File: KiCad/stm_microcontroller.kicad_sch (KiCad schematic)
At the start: 21 parts, among them J5 USB_C_Receptacle_USB2.0_14P, SW1 SW_Push, SW2 SW_Push, U1 STM32F103C8Tx, Y1 8Mhz

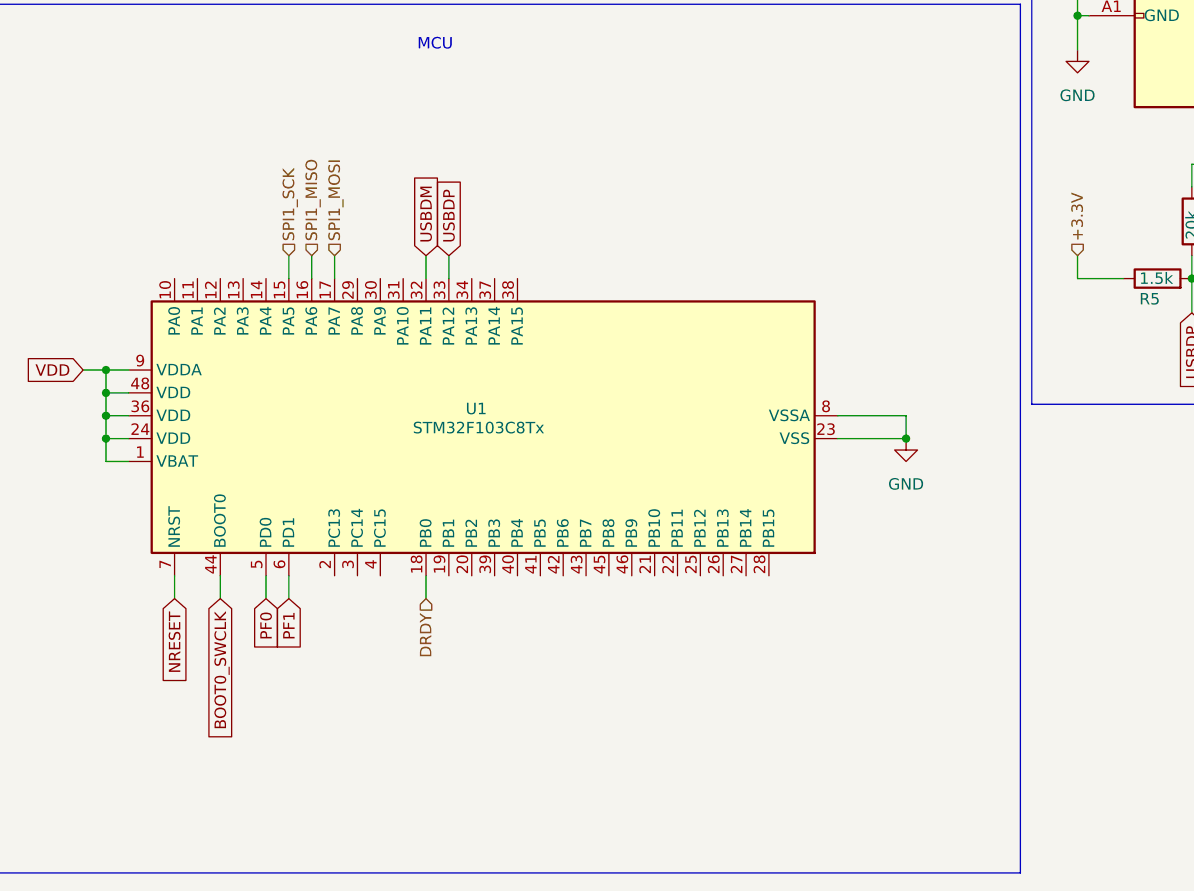
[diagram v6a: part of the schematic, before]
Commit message: Add Single Wire Debug
* Add Single Wire Debug (SWD) Tag Connect Connector
* Re-layout of 5V power so the 5V pins connect to a pad directly behind the USB connector
* Add 0R resistors to air gap the 3.3V and 5V power rails for incremental board bringup
* Rotate ADS1220 for cleaner layout
* Remove connections to reference voltage pins, since AVDD/AVSS is a valid reference

fixup

fixup

fixup
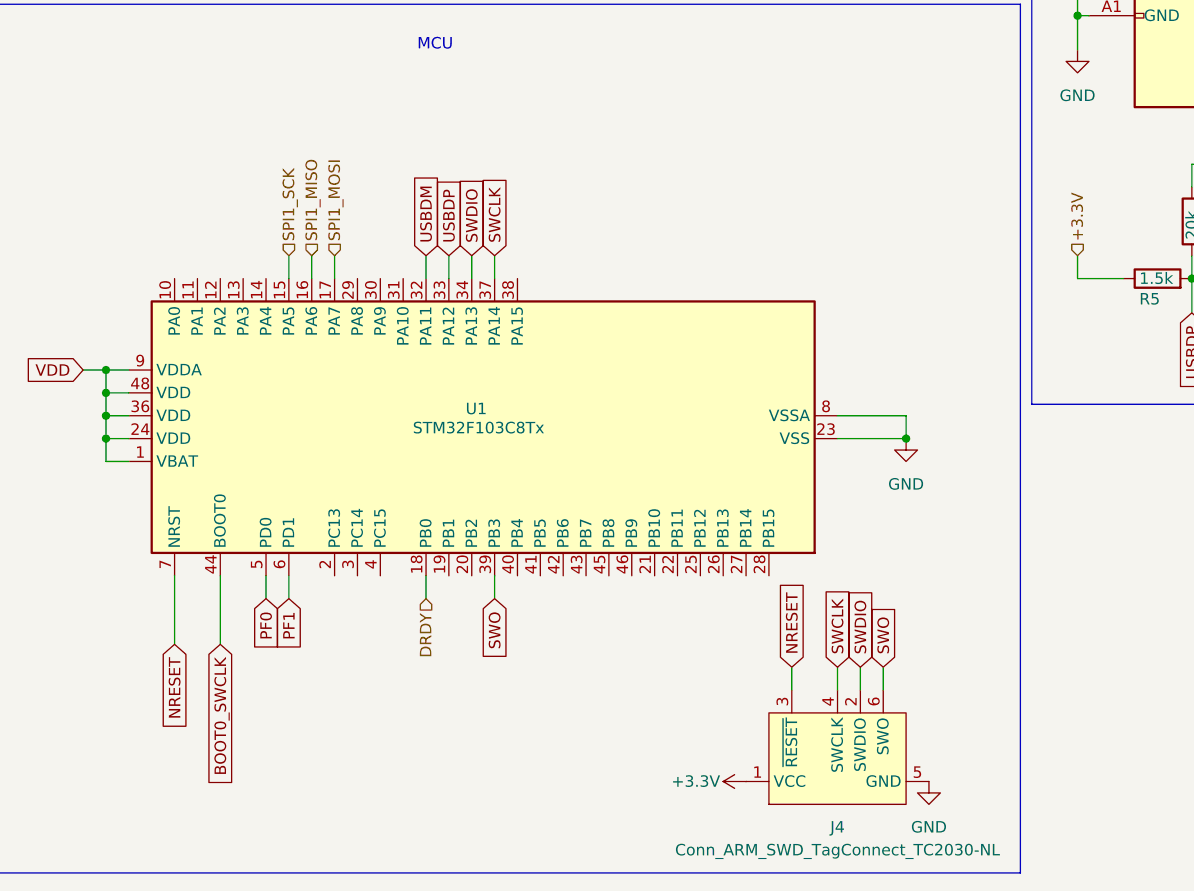
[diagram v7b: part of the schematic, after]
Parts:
- added J4: Conn_ARM_SWD_TagConnect_TC2030-NL, Connector:Tag-Connect_TC2030-IDC-NL_2x03_P1.27mm_Vertical, symbol Connector:Conn_ARM_SWD_TagConnect_TC2030-NL
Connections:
- net +3.3V: now also J4.1 (VCC)
- net GND: now also J4.5 (GND)
- net NRESET: now also J4.3 (~{RESET})
- net SWDIO: now reaches U1.34 (PA13)
- net SWDIO: now also J4.2 (SWDIO)
- net SWCLK: now reaches U1.37 (PA14)
- net SWCLK: now also J4.4 (SWCLK)
- net SWO: now reaches U1.39 (PB3)
- net SWO: now also J4.6 (SWO)

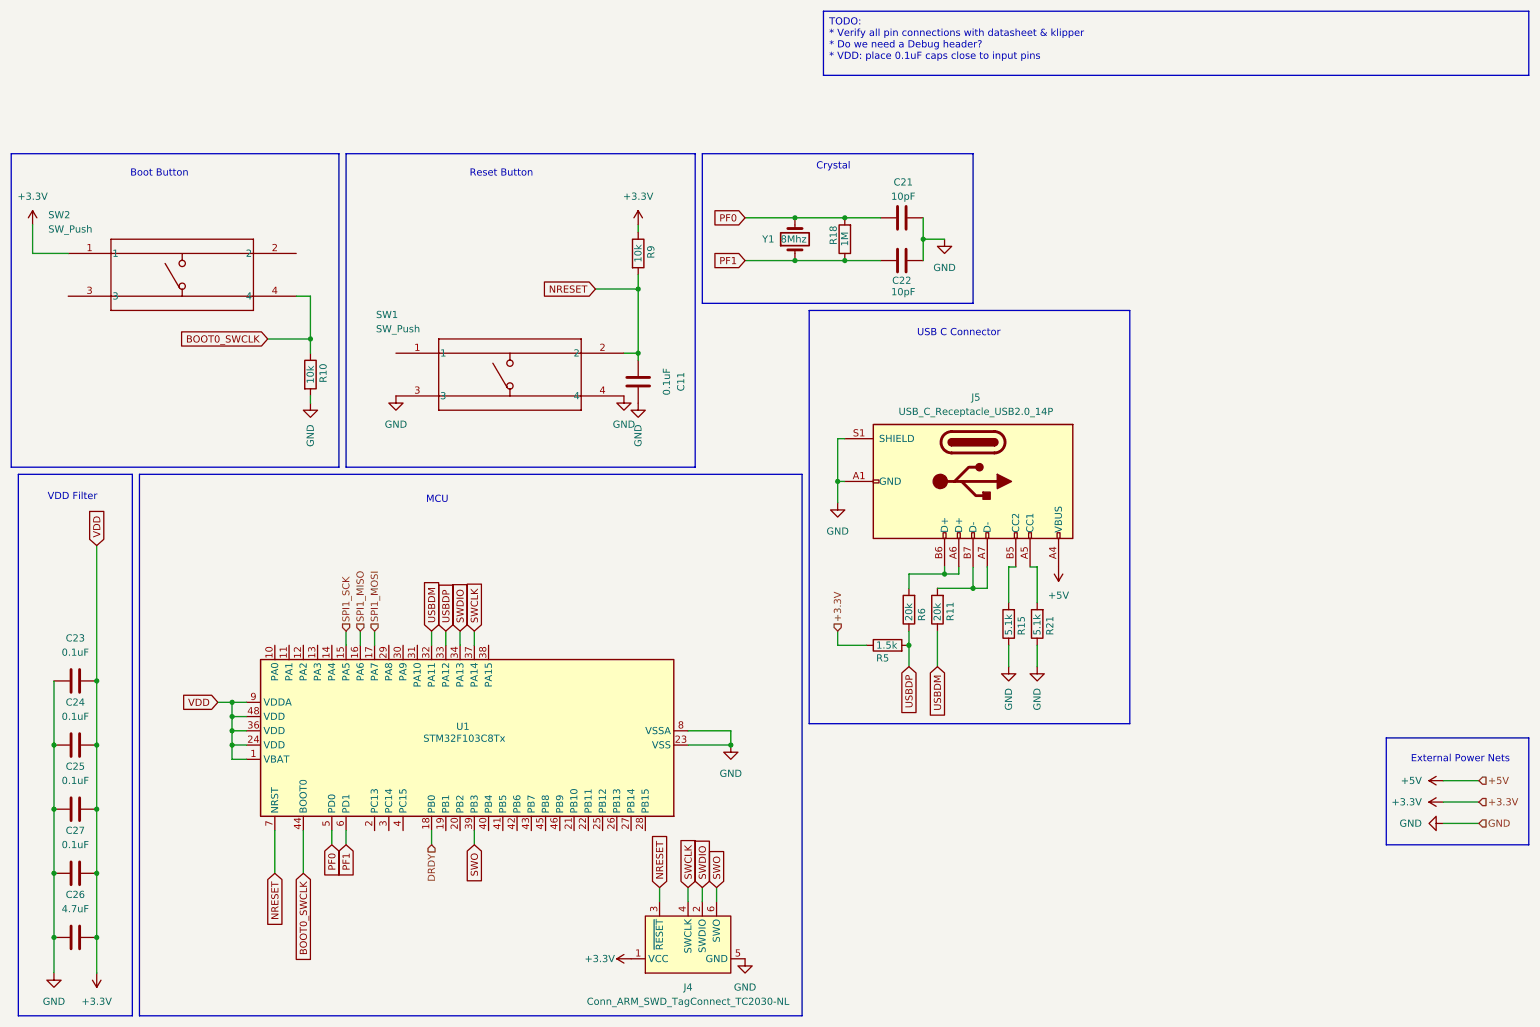
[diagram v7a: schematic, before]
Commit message: USB Improvements
* Changed the USB connector symbol and rebuilt it to have pins that match the pads
* Set up the USB lines as a differential pair
* VIA Stitch the board
* Increased minimum trace width to 0.3mm
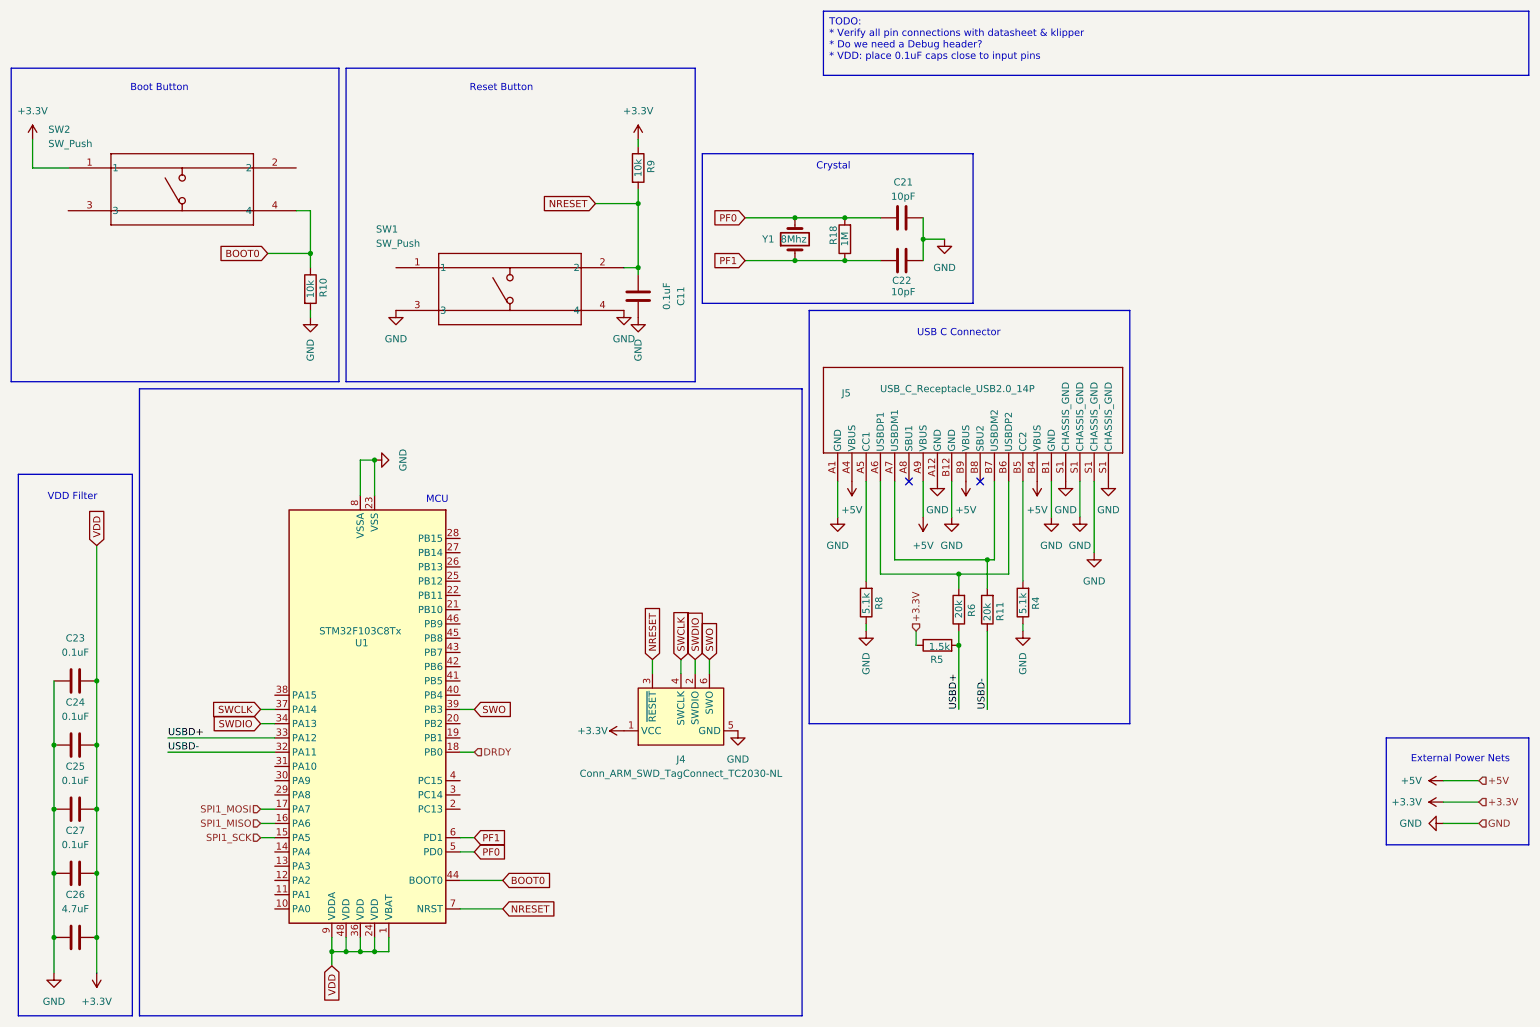
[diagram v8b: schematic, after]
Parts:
- removed R15, R21: 5.1k, Resistor_SMD:R_0805_2012Metric_Pad1.20x1.40mm_HandSolder, symbol Device:R
- added R4, R8: 5.1k, Resistor_SMD:R_0805_2012Metric_Pad1.20x1.40mm_HandSolder, symbol Device:R
- J5: footprint Connector_USB:USB_C_Receptacle_GCT_USB4085 -> CONN16_USB4085-GF-A_GCT; symbol Connector:USB_C_Receptacle_USB2.0_14P -> USB4085_GF_A:USB4085-GF-A
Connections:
- net GND: now also R4.1, R8.1
- net at J5.A5 (CC1): now also R8.2
- net at J5.B5 (CC2): now also R4.2
- net BOOT0_SWCLK renamed BOOT0
- net USBDM renamed USBD-
- net USBDP renamed USBD+
- no-connect marks 0 -> 2
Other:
- moved on the sheet: C11, J4, R10, R11, R5, R6, R9, SW1, SW2, U1
